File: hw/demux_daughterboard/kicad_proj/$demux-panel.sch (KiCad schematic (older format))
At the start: 28 parts, among them P1 CONN_2, P10 CONN_2, P2 CONN_8X2, P3 CONN_8X2, P4 CONN_3X2, P5 CONN_5X2, P6 CONN_5X2, P7 CONN_2, P8 CONN_8X2, P9 CONN_8X2

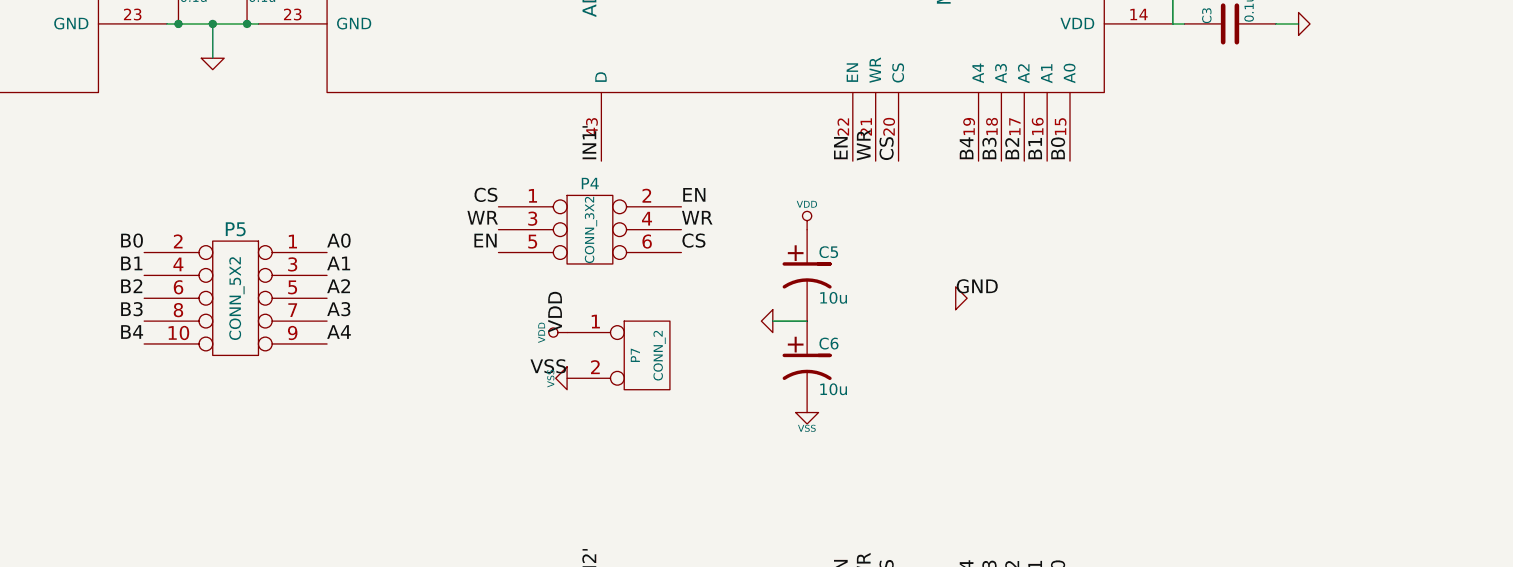
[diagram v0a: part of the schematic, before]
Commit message: Finished daughterboard pcb with fusion pcb constraints, TODO: silkscreen
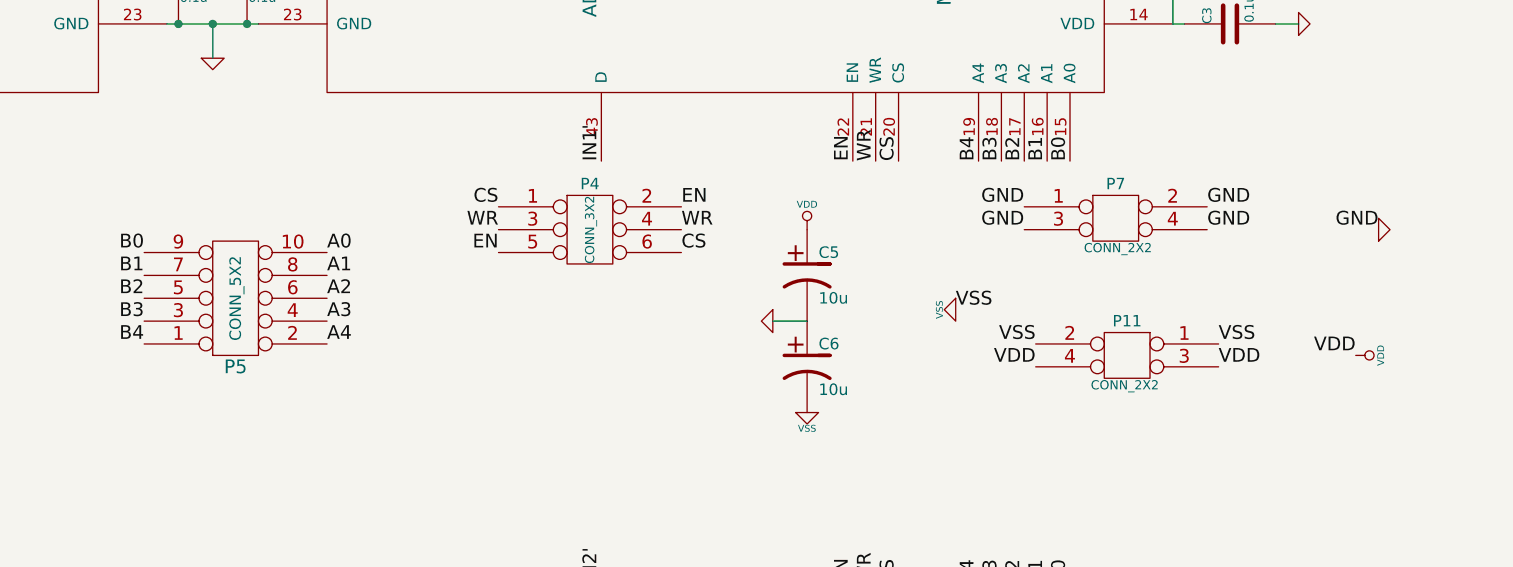
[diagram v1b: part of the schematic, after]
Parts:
- removed P7: CONN_2, symbol CONN_2
- added P11, P7: CONN_2X2, symbol CONN_2X2
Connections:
- net A0: now also P5.10; no longer P5.1
- net A1: now also P5.8; no longer P5.3
- net A2: now also P5.6; no longer P5.5
- net A3: now also P5.4; no longer P5.7
- net A4: now also P5.2; no longer P5.9
- net B0: now also P5.9; no longer P5.2
- net B1: now also P5.7; no longer P5.4
- net B2: now also P5.5; no longer P5.6
- net B3: now also P5.3; no longer P5.8
- net B4: now also P5.1; no longer P5.10
- net GND: now also P7.1, P7.2, P7.3, P7.4
- net VDD: now also P11.3, P11.4
- net VSS: now also P11.1, P11.2
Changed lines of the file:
@@
 L VSS #PWR04
 U 1 1 53239D3F
-P 6700 3850
-F 0 "#PWR04" H 6700 3850 30  0001 C CNN
-F 1 "VSS" H 6700 3780 30  0000 C CNN
-F 2 "" H 6700 3850 60  0001 C CNN
-F 3 "" H 6700 3850 60  0001 C CNN
-	1    6700 3850
+P 8400 3550
+F 0 "#PWR04" H 8400 3550 30  0001 C CNN
+F 1 "VSS" H 8400 3480 30  0000 C CNN
+F 2 "" H 8400 3550 60  0001 C CNN
+F 3 "" H 8400 3550 60  0001 C CNN
+	1    8400 3550
 	0    1    1    0
 $EndComp
@@
 L GND #PWR05
 U 1 1 53239D45
-P 8400 3500
-F 0 "#PWR05" H 8400 3500 30  0001 C CNN
-F 1 "GND" H 8400 3430 30  0001 C CNN
-F 2 "" H 8400 3500 60  0001 C CNN
-F 3 "" H 8400 3500 60  0001 C CNN
-	1    8400 3500
+P 10250 3200
+F 0 "#PWR05" H 10250 3200 30  0001 C CNN
+F 1 "GND" H 10250 3130 30  0001 C CNN
+F 2 "" H 10250 3200 60  0001 C CNN
+F 3 "" H 10250 3200 60  0001 C CNN
+	1    10250 3200
 	0    -1   -1   0
 $EndComp
@@
 L VDD #PWR06
 U 1 1 53239D4B
-P 6700 3650
-F 0 "#PWR06" H 6700 3750 30  0001 C CNN
-F 1 "VDD" H 6700 3760 30  0000 C CNN
-F 2 "" H 6700 3650 60  0001 C CNN
-F 3 "" H 6700 3650 60  0001 C CNN
-	1    6700 3650
-	0    -1   -1   0
-$EndComp
-Text Label 8400 3500 0    60   ~ 0
+P 10150 3750
+F 0 "#PWR06" H 10150 3850 30  0001 C CNN
+F 1 "VDD" H 10150 3860 30  0000 C CNN
+F 2 "" H 10150 3750 60  0001 C CNN
+F 3 "" H 10150 3750 60  0001 C CNN
+	1    10150 3750
+	0    1    1    0
+$EndComp
+Text Label 8700 3100 2    60   ~ 0
 GND
-Text Label 6700 3850 2    60   ~ 0
+Text Label 9550 3700 0    60   ~ 0
 VSS
-Text Label 6700 3650 1    60   ~ 0
+Text Label 9550 3800 0    60   ~ 0
 VDD
 Text Label 6400 3100 2    60   ~ 0
@@
 Text Label 7200 3100 0    60   ~ 0
 EN
-$Comp
-L CONN_2 P7
-U 1 1 53239FDE
-P 7050 3750
-F 0 "P7" V 7000 3750 40  0000 C CNN
-F 1 "CONN_2" V 7100 3750 40  0000 C CNN
-F 2 "" H 7050 3750 60  0000 C CNN
-F 3 "" H 7050 3750 60  0000 C CNN
-	1    7050 3750
-	1    0    0    -1
-$EndComp
 $Comp
 L CONN_8X2 P3
@@
 F 3 "" H 5250 3500 60  0000 C CNN
 	1    5250 3500
-	-1   0    0    -1
+	1    0    0    1
 $EndComp
 Text Label 5650 3300 0    60   ~ 0
 A0
+$Comp
+L CONN_2X2 P7
+U 1 1 5326173E
+P 9100 3150
+F 0 "P7" H 9100 3300 50  0000 C CNN
+F 1 "CONN_2X2" H 9110 3020 40  0000 C CNN
+F 2 "" H 9100 3150 60  0000 C CNN
+F 3 "" H 9100 3150 60  0000 C CNN
+	1    9100 3150
+	1    0    0    -1
+$EndComp
+$Comp
+L CONN_2X2 P11
+U 1 1 5326174D
+P 9150 3750
+F 0 "P11" H 9150 3900 50  0000 C CNN
+F 1 "CONN_2X2" H 9160 3620 40  0000 C CNN
+F 2 "" H 9150 3750 60  0000 C CNN
+F 3 "" H 9150 3750 60  0000 C CNN
+	1    9150 3750
+	-1   0    0    -1
+$EndComp
+Text Label 8700 3200 2    60   ~ 0
+GND
+Text Label 10250 3200 2    60   ~ 0
+GND
+Text Label 9500 3200 0    60   ~ 0
+GND
+Text Label 9500 3100 0    60   ~ 0
+GND
+Text Label 8750 3800 2    60   ~ 0
+VDD
+Text Label 8750 3700 2    60   ~ 0
+VSS
+Text Label 10150 3750 2    60   ~ 0
+VDD
+Text Label 8400 3550 0    60   ~ 0
+VSS
 $EndSCHEMATC
